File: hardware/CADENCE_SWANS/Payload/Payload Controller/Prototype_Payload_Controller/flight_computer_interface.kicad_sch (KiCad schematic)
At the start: 0 parts

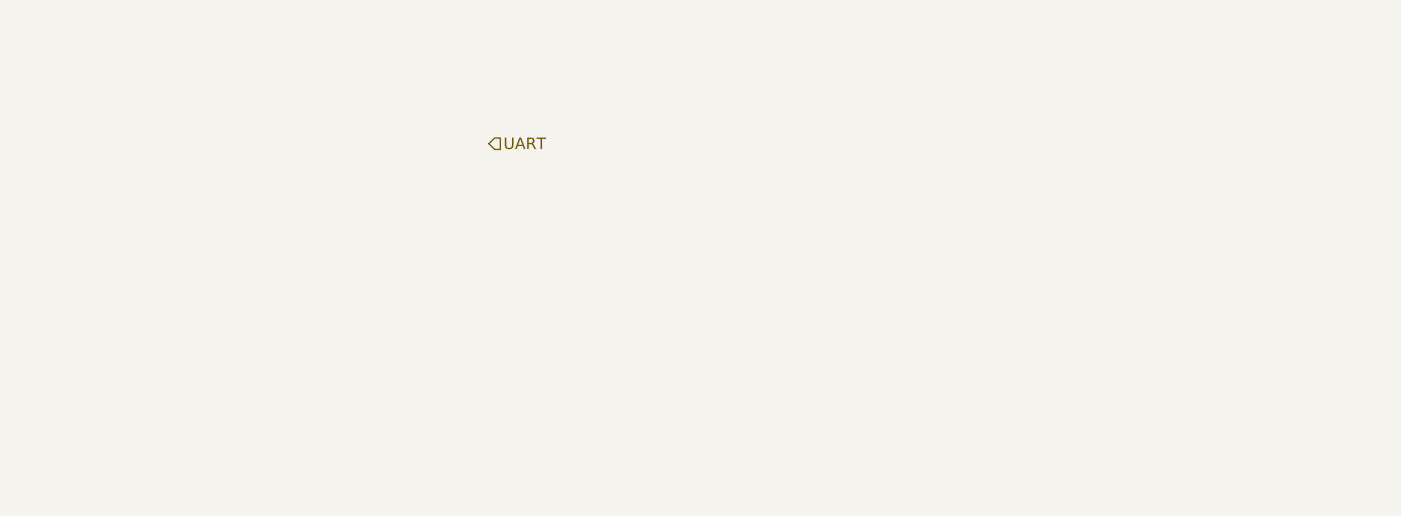
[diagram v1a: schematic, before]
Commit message: added SN65C1668 symbol library and a folder for symbols
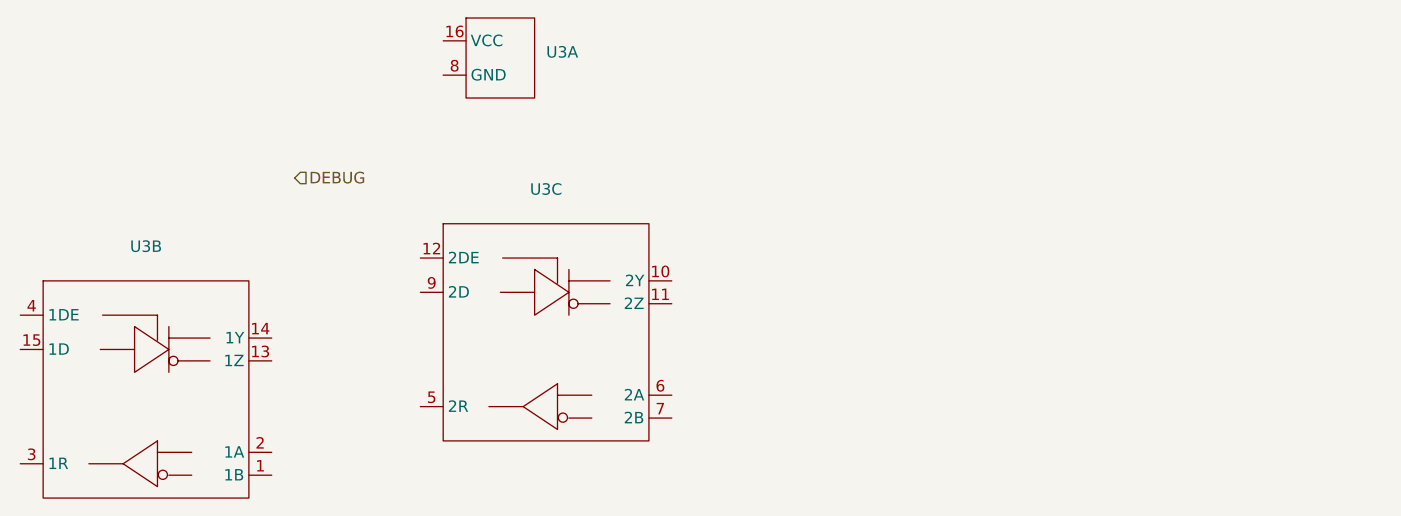
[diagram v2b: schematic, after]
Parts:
- added U3: ~, symbol SN65C1168:SN65C1168

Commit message: updates
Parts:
- removed U3: ~, symbol SN65C1168:SN65C1168

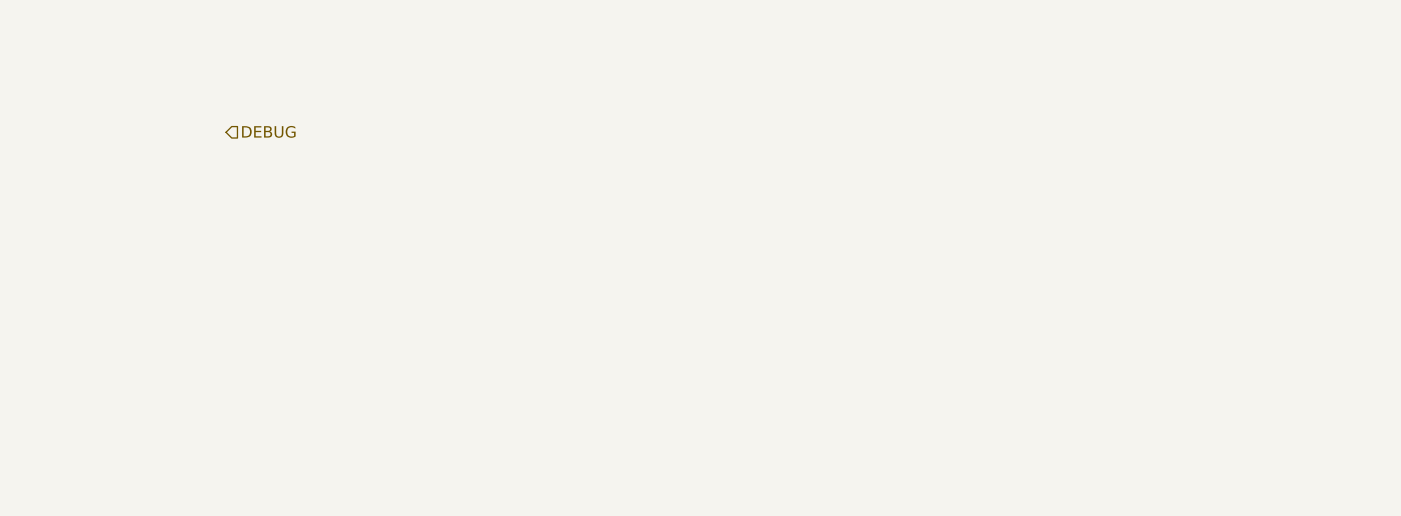
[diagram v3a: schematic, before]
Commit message: updated schematic symbol
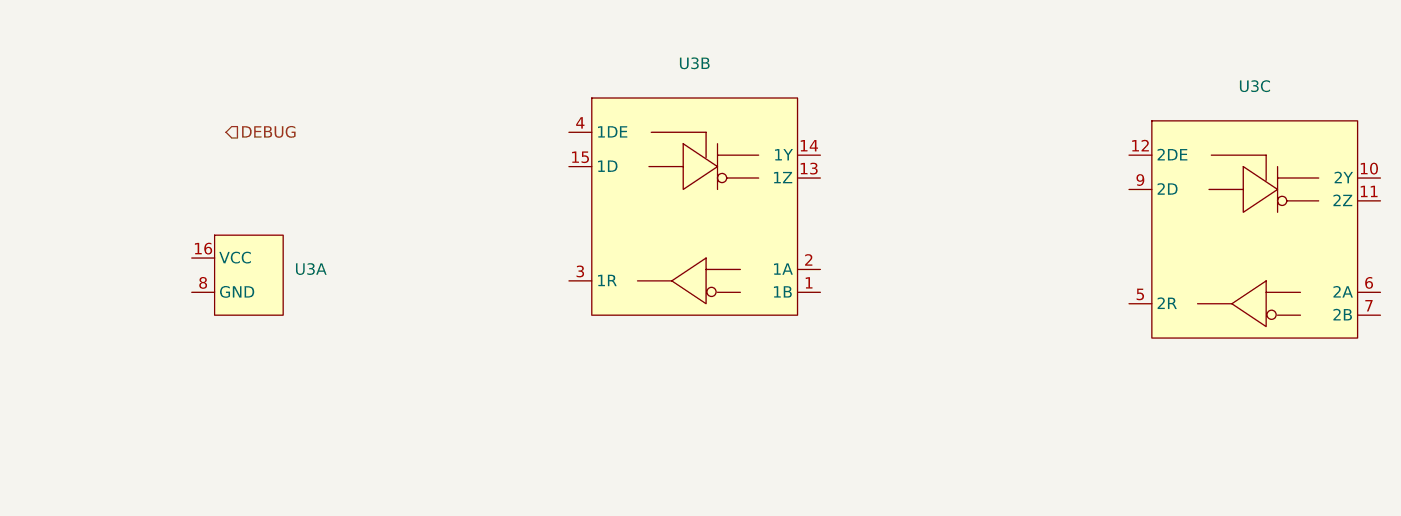
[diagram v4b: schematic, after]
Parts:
- added U3: ~, symbol SN65C1168:SN65C1168
